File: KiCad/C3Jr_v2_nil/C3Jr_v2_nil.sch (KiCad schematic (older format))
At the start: 37 parts, among them P1 CONN_1, P2 CONN_1, P3 CONN_1, P4 CONN_1, P5 DC_IN_1, P6 DC_IN_2, P7 DIL6, P8 DIL6, P9 DIL6, Q1 PBSS9110Z

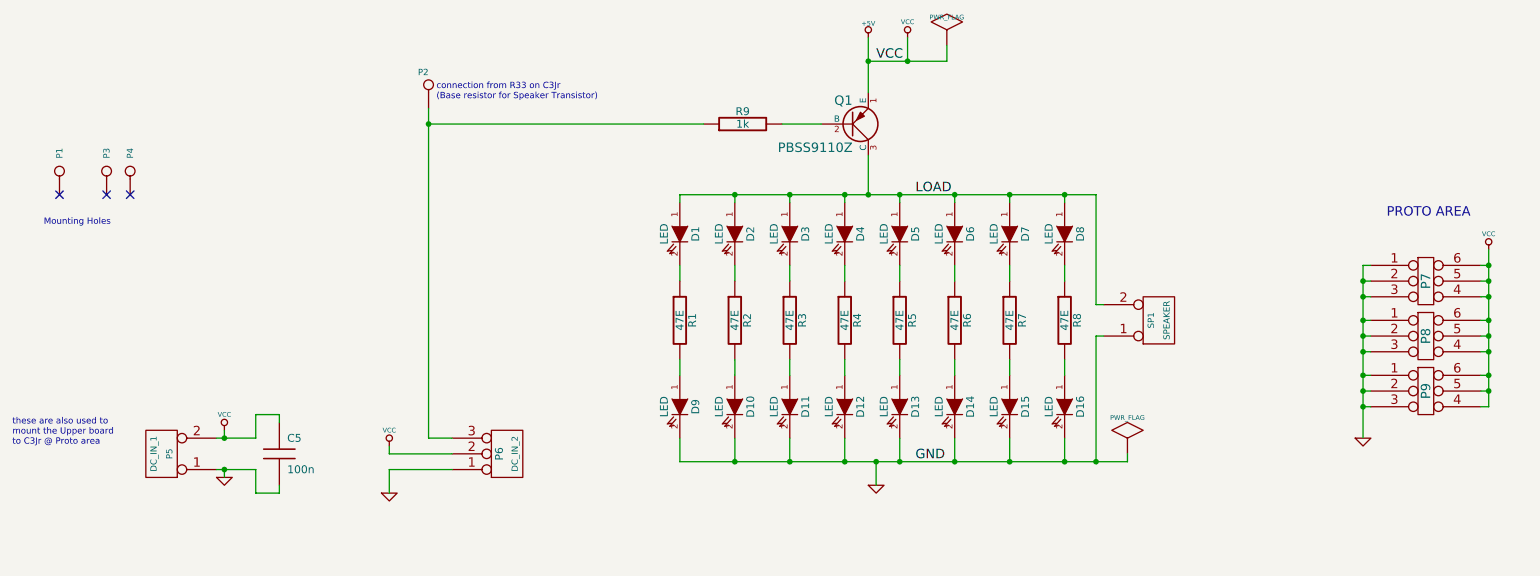
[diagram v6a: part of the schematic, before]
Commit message: C3Jr_v2_nil : added LEDs, reduced board size,
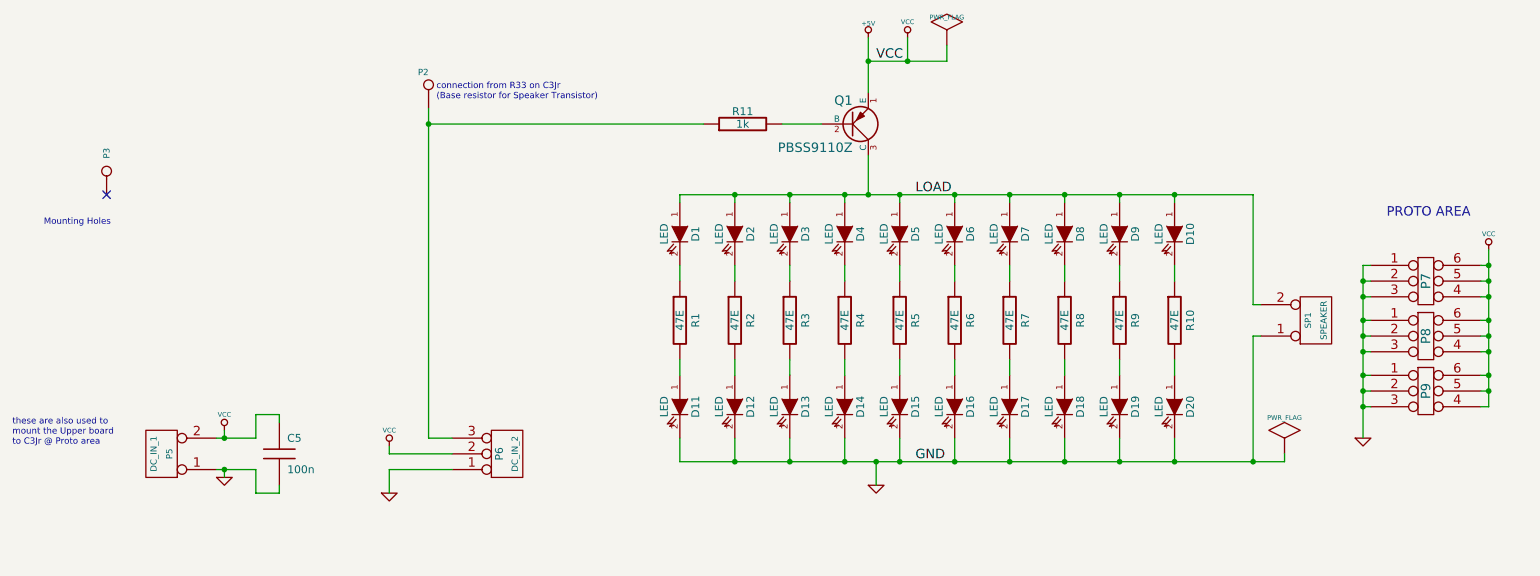
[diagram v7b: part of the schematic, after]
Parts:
- removed P1, P4: CONN_1, symbol CONN_1
- added D10, D19, D20, D9: LED, symbol LED
- added R10, R9: 47E, symbol R
- renumbered D9 to D11, D10 to D12, D11 to D13, D12 to D14, D13 to D15, D14 to D16, D15 to D17, D16 to D18, R9 to R11
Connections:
- net GND: now also D19.2 (K), D20.2 (K)
- net LOAD: now also D10.1 (A), D9.1 (A)
- new net: D10.2 (K), R10.1
- new net: D20.1 (A), R10.2
- new net: D9.2 (K), R9.1
- new net: D19.1 (A), R9.2
- no-connect marks 3 -> 1
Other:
- moved on the sheet: SP1
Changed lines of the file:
@@
-EESchema Schematic File Version 2  date Sunday 06 May 2012 12:23:57 AM IST
+EESchema Schematic File Version 2  date 5/28/2012 12:53:29 PM
 LIBS:C3Jr_v2_nil
 LIBS:ATtiny85_bmp
@@
 Sheet 1 1
 Title ""
-Date "5 may 2012"
+Date "28 may 2012"
 Rev ""
 Comp ""
@@
 Comment4 ""
 $EndDescr
-Text Notes 4050 1100 0    40   ~ 0
-connection from R33 on C3Jr\n(Base resistor for Speaker Transistor)
+Connection ~ 8750 3400
+Wire Wire Line
+	8750 3250 8750 3400
+Connection ~ 8750 1700
+Wire Wire Line
+	8750 1750 8750 1700
+Wire Wire Line
+	8750 2150 8750 2250
+Wire Wire Line
+	8750 2750 8750 2850
+Wire Wire Line
+	8400 2750 8400 2850
+Wire Wire Line
+	8400 2150 8400 2250
 Connection ~ 4000 1250
 Wire Wire Line
@@
 Connection ~ 8050 1700
 Wire Wire Line
-	8250 1700 5600 1700
-Wire Wire Line
-	8250 1700 8250 2400
-Wire Wire Line
-	8250 2400 8300 2400
+	9250 1700 5600 1700
+Wire Wire Line
+	9250 1700 9250 2400
+Wire Wire Line
+	9250 2400 9300 2400
 Connection ~ 2700 3450
 Wire Wire Line
@@
 	6250 1250 6500 1250
 Wire Wire Line
-	6800 1050 6800 700
+	6800 700  6800 1050
 Wire Wire Line
 	7700 1700 7700 1750
@@
 Connection ~ 10750 2700
 Wire Wire Line
-	10750 2950 10700 2950
+	10700 2950 10750 2950
 Connection ~ 10750 2950
 Wire Wire Line
-	8300 2600 8250 2600
-Wire Wire Line
-	8250 2600 8250 3400
+	9300 2600 9250 2600
+Wire Wire Line
+	9250 2600 9250 3400
 Connection ~ 8050 3400
 Wire Wire Line
-	4000 1250 5750 1250
+	5750 1250 4000 1250
 Wire Wire Line
 	4000 3250 4150 3250
 Wire Wire Line
-	8450 3350 8450 3400
-Wire Wire Line
-	8450 3400 5600 3400
-Connection ~ 8250 3400
+	9450 3350 9450 3400
+Wire Wire Line
+	9450 3400 5600 3400
+Connection ~ 9250 3400
+Wire Wire Line
+	8400 1750 8400 1700
+Connection ~ 8400 1700
+Wire Wire Line
+	8400 3250 8400 3400
+Connection ~ 8400 3400
+$Comp
+L LED D10
+U 1 1 4FC32749
+P 8750 1950
+F 0 "D10" H 8750 2050 50  0000 C CNN
+F 1 "LED" H 8750 1850 50  0000 C CNN
+	1    8750 1950
+	0    1    1    0
+$EndComp
+$Comp
+L LED D20
+U 1 1 4FC32748
+P 8750 3050
+F 0 "D20" H 8750 3150 50  0000 C CNN
+F 1 "LED" H 8750 2950 50  0000 C CNN
+	1    8750 3050
+	0    1    1    0
+$EndComp
+$Comp
+L LED D19
+U 1 1 4FC32747
+P 8400 3050
+F 0 "D19" H 8400 3150 50  0000 C CNN
+F 1 "LED" H 8400 2950 50  0000 C CNN
+	1    8400 3050
+	0    1    1    0
+$EndComp
+$Comp
+L LED D9
+U 1 1 4FC32746
+P 8400 1950
+F 0 "D9" H 8400 2050 50  0000 C CNN
+F 1 "LED" H 8400 1850 50  0000 C CNN
+	1    8400 1950
+	0    1    1    0
+$EndComp
+$Comp
+L R R9
+U 1 1 4FC32745
+P 8400 2500
+F 0 "R9" V 8500 2500 50  0000 C CNN
+F 1 "47E" V 8400 2500 50  0000 C CNN
+	1    8400 2500
+	1    0    0    -1
+$EndComp
+$Comp
+L R R10
+U 1 1 4FC32744
+P 8750 2500
+F 0 "R10" V 8850 2500 50  0000 C CNN
+F 1 "47E" V 8750 2500 50  0000 C CNN
+	1    8750 2500
+	1    0    0    -1
+$EndComp
+Text Notes 4050 1100 0    40   ~ 0
+connection from R33 on C3Jr\n(Base resistor for Speaker Transistor)
 Text Notes 7050 6300 0    60   ~ 12
 C3Jr-Name-in-Lights\n------------------------\nan array of 16 SMD LEDs driven either via Speaker Transistor on C3Jr\nusing SP1 for control signal and P5/P6 for Power (+5V, GND)\nOR, by using on board Transistor with Base Resistor, via any other\navailable control pin on the controller.\nIf using on-board Transistor, Pin 3 of connector P6 gets terminated\non Proto Area, and can be red-wired to appropriate control pin.
@@
 NoConn ~ 1950 1700
 $Comp
-L CONN_1 P4
-U 1 1 4FA3BE35
-P 2100 1550
-F 0 "P4" H 2180 1550 40  0000 L CNN
-F 1 "CONN_1" H 2100 1605 30  0001 C CNN
-	1    2100 1550
-	0    -1   -1   0
-$EndComp
-NoConn ~ 2100 1700
-$Comp
 L PWR_FLAG #FLG01
 U 1 1 4FA3BD94
-P 8450 3350
-F 0 "#FLG01" H 8450 3620 30  0001 C CNN
-F 1 "PWR_FLAG" H 8450 3580 30  0000 C CNN
-	1    8450 3350
+P 9450 3350
+F 0 "#FLG01" H 9450 3620 30  0001 C CNN
+F 1 "PWR_FLAG" H 9450 3580 30  0000 C CNN
+	1    9450 3350
 	1    0    0    -1
 $EndComp
@@
 L CONN_2 SP1
 U 1 1 4F9EE042
-P 8650 2500
-F 0 "SP1" V 8600 2500 40  0000 C CNN
-F 1 "SPEAKER" V 8700 2500 40  0000 C CNN
-	1    8650 2500
+P 9650 2500
+F 0 "SP1" V 9600 2500 40  0000 C CNN
+F 1 "SPEAKER" V 9700 2500 40  0000 C CNN
+	1    9650 2500
 	1    0    0    1
 $EndComp
@@
 Text Notes 1550 1900 0    40   ~ 0
 Mounting Holes
-NoConn ~ 1650 1700
-$Comp
-L CONN_1 P1
-U 1 1 4F9ED31D
-P 1650 1550
-F 0 "P1" H 1730 1550 40  0000 L CNN
-F 1 "CONN_1" H 1650 1605 30  0001 C CNN
-	1    1650 1550
-	0    -1   -1   0
-$EndComp
 $Comp
 L C C5
@@
 $EndComp
 $Comp
-L R R9
+L R R11
 U 1 1 4F1561DE
 P 6000 1250
-F 0 "R9" V 6080 1250 50  0000 C CNN
+F 0 "R11" V 6080 1250 50  0000 C CNN
 F 1 "1k" V 6000 1250 50  0000 C CNN
 	1    6000 1250
@@
 U 1 1 4F15611D
 P 8050 2500
-F 0 "R8" V 8130 2500 50  0000 C CNN
+F 0 "R8" V 8150 2500 50  0000 C CNN
 F 1 "47E" V 8050 2500 50  0000 C CNN
 	1    8050 2500
@@
 U 1 1 4F15611B
 P 7700 2500
-F 0 "R7" V 7780 2500 50  0000 C CNN
+F 0 "R7" V 7800 2500 50  0000 C CNN
 F 1 "47E" V 7700 2500 50  0000 C CNN
 	1    7700 2500
@@
 U 1 1 4F15611A
 P 7350 2500
-F 0 "R6" V 7430 2500 50  0000 C CNN
+F 0 "R6" V 7450 2500 50  0000 C CNN
 F 1 "47E" V 7350 2500 50  0000 C CNN
 	1    7350 2500
@@
 U 1 1 4F156118
 P 7000 2500
-F 0 "R5" V 7080 2500 50  0000 C CNN
+F 0 "R5" V 7100 2500 50  0000 C CNN
 F 1 "47E" V 7000 2500 50  0000 C CNN
 	1    7000 2500
@@
 U 1 1 4F156116
 P 6650 2500
-F 0 "R4" V 6730 2500 50  0000 C CNN
+F 0 "R4" V 6750 2500 50  0000 C CNN
 F 1 "47E" V 6650 2500 50  0000 C CNN
 	1    6650 2500
@@
 U 1 1 4F156115
 P 6300 2500
-F 0 "R3" V 6380 2500 50  0000 C CNN
+F 0 "R3" V 6400 2500 50  0000 C CNN
 F 1 "47E" V 6300 2500 50  0000 C CNN
 	1    6300 2500
@@
 U 1 1 4F156113
 P 5950 2500
-F 0 "R2" V 6030 2500 50  0000 C CNN
+F 0 "R2" V 6050 2500 50  0000 C CNN
 F 1 "47E" V 5950 2500 50  0000 C CNN
 	1    5950 2500
@@
 U 1 1 4F15610E
 P 5600 2500
-F 0 "R1" V 5680 2500 50  0000 C CNN
+F 0 "R1" V 5700 2500 50  0000 C CNN
 F 1 "47E" V 5600 2500 50  0000 C CNN
 	1    5600 2500
@@
 $EndComp
 $Comp
-L LED D13
+L LED D15
 U 1 1 4F155F20
 P 7000 3050
-F 0 "D13" H 7000 3150 50  0000 C CNN
+F 0 "D15" H 7000 3150 50  0000 C CNN
 F 1 "LED" H 7000 2950 50  0000 C CNN
 	1    7000 3050
@@
 $EndComp
 $Comp
-L LED D14
+L LED D16
 U 1 1 4F155F1E
 P 7350 3050
-F 0 "D14" H 7350 3150 50  0000 C CNN
+F 0 "D16" H 7350 3150 50  0000 C CNN
 F 1 "LED" H 7350 2950 50  0000 C CNN
 	1    7350 3050
@@
 $EndComp
 $Comp
-L LED D15
+L LED D17
 U 1 1 4F155F1C
 P 7700 3050
-F 0 "D15" H 7700 3150 50  0000 C CNN
+F 0 "D17" H 7700 3150 50  0000 C CNN
 F 1 "LED" H 7700 2950 50  0000 C CNN
 	1    7700 3050
@@
 $EndComp
 $Comp
-L LED D16
+L LED D18
 U 1 1 4F155F1B
 P 8050 3050
-F 0 "D16" H 8050 3150 50  0000 C CNN
+F 0 "D18" H 8050 3150 50  0000 C CNN
 F 1 "LED" H 8050 2950 50  0000 C CNN
 	1    8050 3050
@@
 $EndComp
 $Comp
-L LED D12
+L LED D14
 U 1 1 4F155EF1
 P 6650 3050
-F 0 "D12" H 6650 3150 50  0000 C CNN
+F 0 "D14" H 6650 3150 50  0000 C CNN
 F 1 "LED" H 6650 2950 50  0000 C CNN
 	1    6650 3050
@@
 $EndComp
 $Comp
-L LED D11
+L LED D13
 U 1 1 4F155EEF
 P 6300 3050
-F 0 "D11" H 6300 3150 50  0000 C CNN
+F 0 "D13" H 6300 3150 50  0000 C CNN
 F 1 "LED" H 6300 2950 50  0000 C CNN
 	1    6300 3050
@@
 $EndComp
 $Comp
-L LED D10
+L LED D12
 U 1 1 4F155EB8
 P 5950 3050
-F 0 "D10" H 5950 3150 50  0000 C CNN
+F 0 "D12" H 5950 3150 50  0000 C CNN
 F 1 "LED" H 5950 2950 50  0000 C CNN
 	1    5950 3050
@@
 $EndComp
 $Comp
-L LED D9
+L LED D11
 U 1 1 4F155EA3
 P 5600 3050
-F 0 "D9" H 5600 3150 50  0000 C CNN
+F 0 "D11" H 5600 3150 50  0000 C CNN
 F 1 "LED" H 5600 2950 50  0000 C CNN
 	1    5600 3050

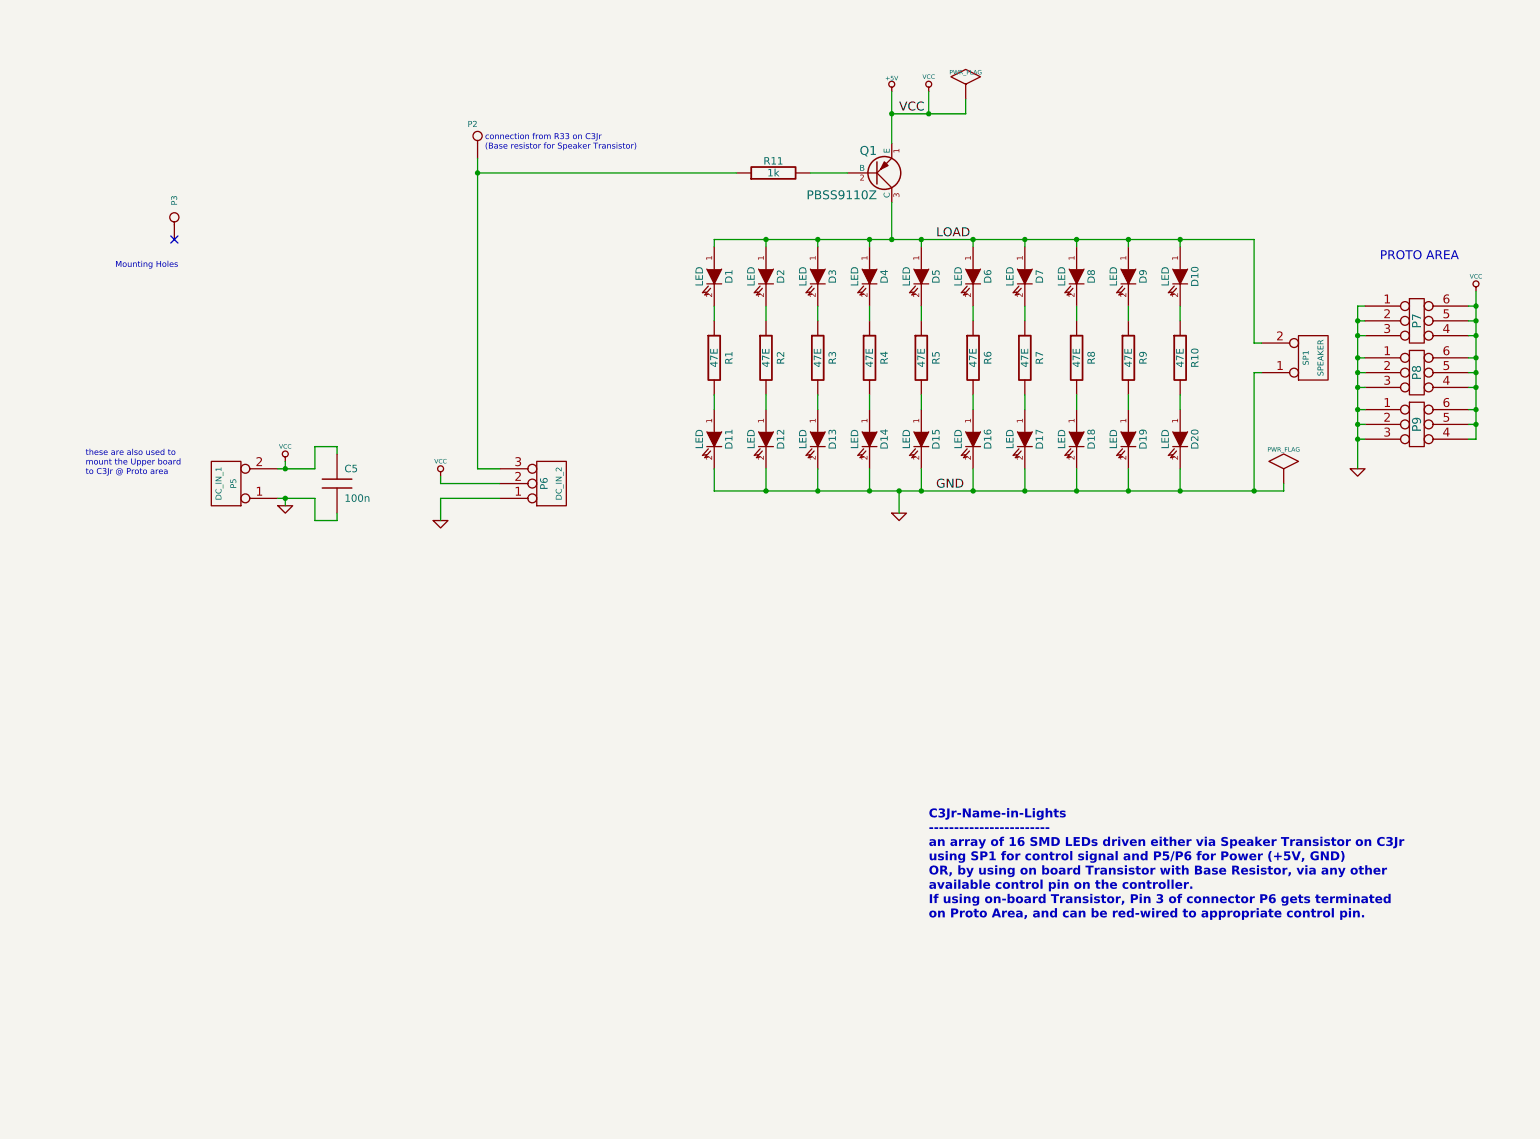
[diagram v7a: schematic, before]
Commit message: C3Jr_v2_nil : changed layout. Single LED instead of a pair in each limb.
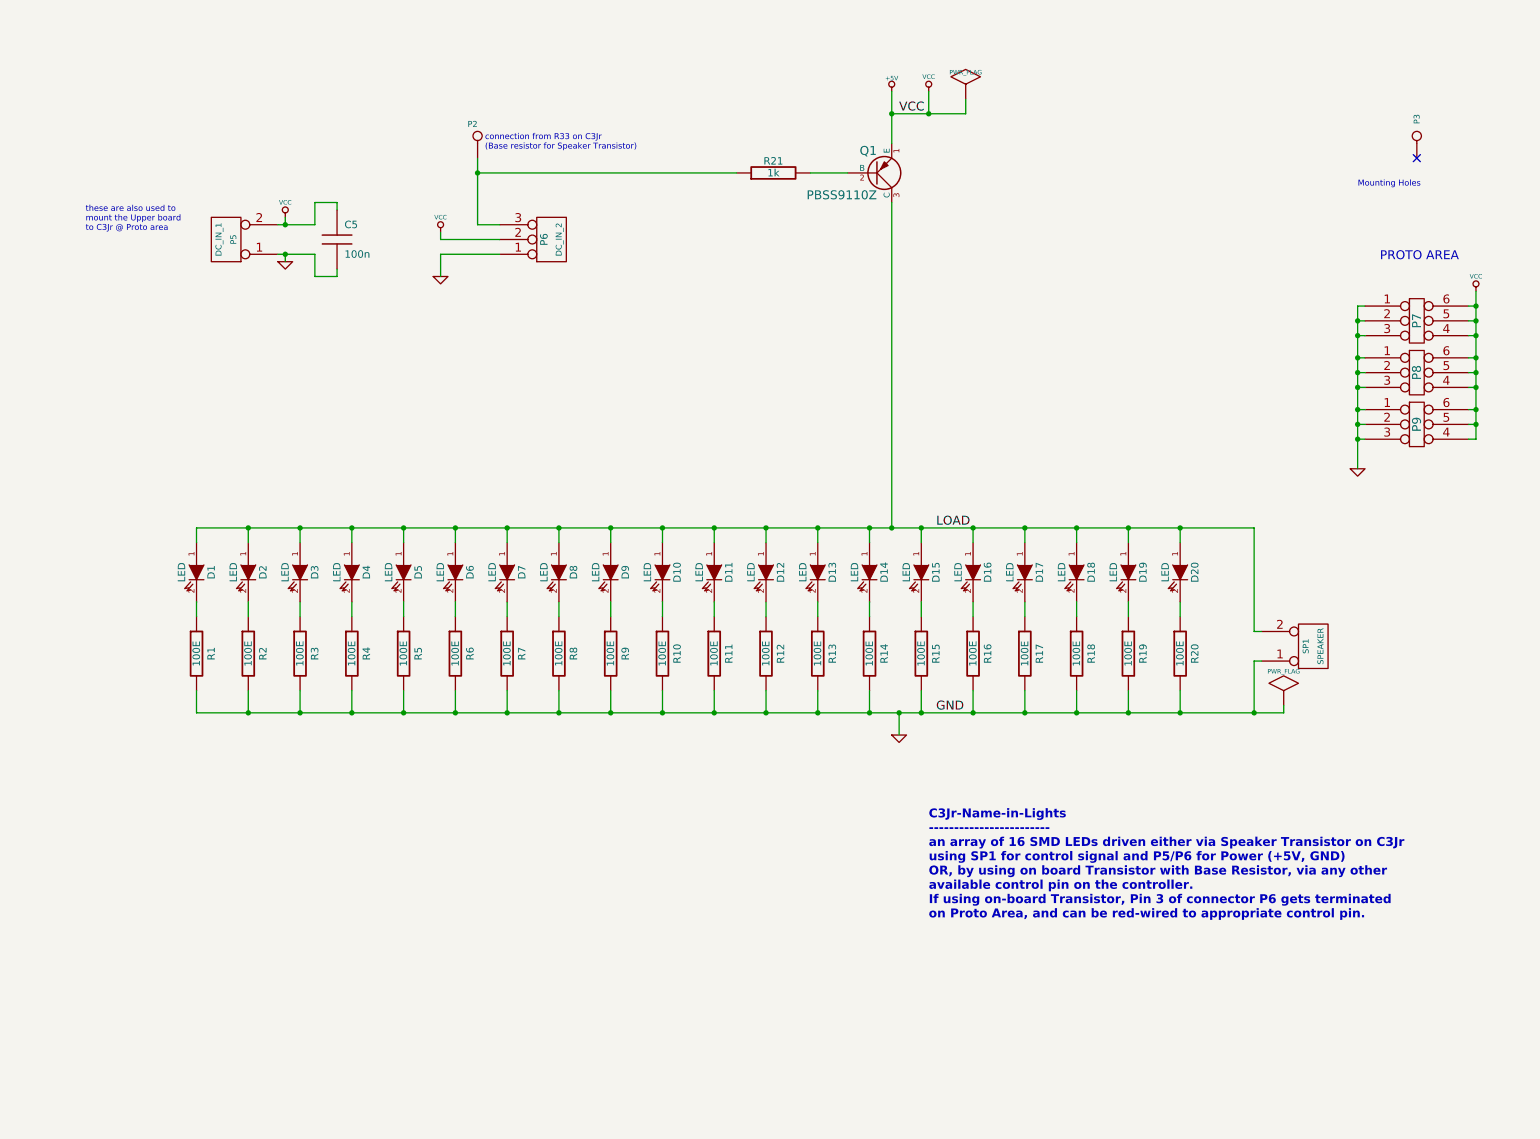
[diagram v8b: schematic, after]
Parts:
- added R11, R12, R13, R14, R15, R16, R17, R18, R19, R20: 100E, symbol R
- R1, R10, R2, R3, R4, R5, R6, R7, R8, R9: value 47E -> 100E
- renumbered R11 to R21
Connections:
- net GND: now also R1.2, R10.2, R2.2, R3.2, R4.2, R5.2, R6.2, R7.2, R8.2, R9.2, R11.2, R12.2, R13.2, R14.2, R15.2, R16.2, R17.2, R18.2, R19.2, R20.2; no longer D11.2 (K), D12.2 (K), D13.2 (K), D14.2 (K), D15.2 (K), D16.2 (K), D17.2 (K), D18.2 (K), D19.2 (K), D20.2 (K)
- net LOAD: now also D11.1 (A), D12.1 (A), D13.1 (A), D14.1 (A), D15.1 (A), D16.1 (A), D17.1 (A), D18.1 (A), D19.1 (A), D20.1 (A)
- new net: D11.2 (K), R11.1
- new net: D12.2 (K), R12.1
- new net: D13.2 (K), R13.1
- new net: D14.2 (K), R14.1
- new net: D18.2 (K), R18.1
- new net: D17.2 (K), R17.1
- new net: D16.2 (K), R16.1
- new net: D15.2 (K), R15.1
- new net: D19.2 (K), R19.1
- new net: D20.2 (K), R20.1
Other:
- moved on the sheet: C5, D1, D10, D11, D12, D13, D14, D15, D16, D17, D18, D19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
